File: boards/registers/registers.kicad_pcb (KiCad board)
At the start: 2 copper layers, 100 x 100 mm, 192 parts, among them J1 SSW-120-02-G-D-RA, J2 SSW-120-02-G-D-RA, J4 5V, J5 SSW-120-02-G-D-RA, SW1 RESET, SW2 STEP, SW3 OS102011MS2QN1, U1 SN74ACT08PW, U10 MC74ACT161DG, U11 SN74ACT244PW, U12 SN74ACT244PW, U13 MC74ACT161DG, U14 MC74ACT161DG, U15 SN74ACT244PW, U16 SN74ACT244PW, U17 MC74ACT161DG, U18 MC74ACT161DG, U19 SN74ACT244PW, U2 SN74ACT244PW, U20 SN74ACT244PW, U21 MC74ACT161DG, U22 MC74ACT161DG, U23 SN74ACT244PW, U24 SN74ACT244PW, U25 MC74AC273DTR2G, U26 SN74ACT244PW, U27 SN74ACT244PW, U28 MC74AC273DTR2G, U29 SN74ACT244PW, U3 MC74AC273DTR2G, U34 74ACT14MTCX, U4 MC74ACT161DG, U5 MC74ACT86DG, U6 SN74ACT08PW, U7 SN74ACT32PWR, U8 SN74ACT32PWR, U9 MC74ACT161DG

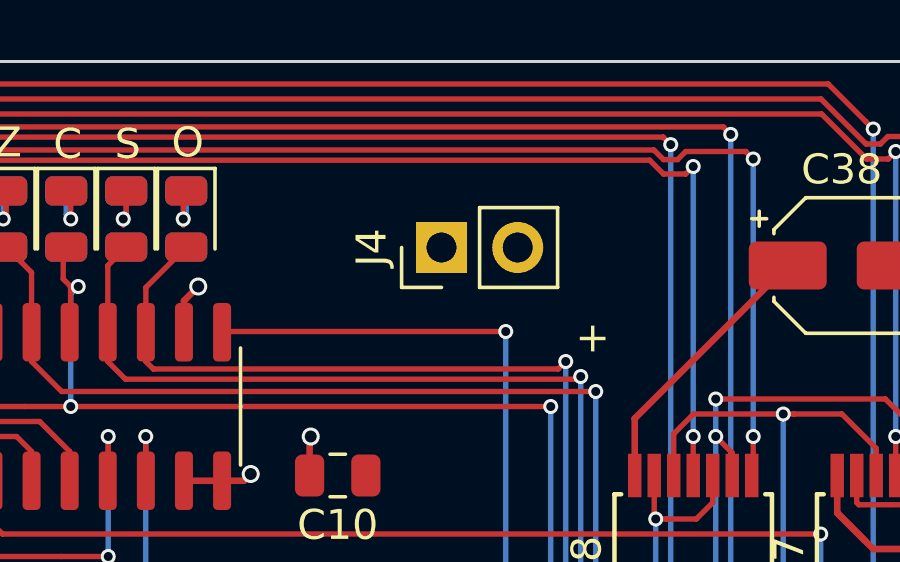
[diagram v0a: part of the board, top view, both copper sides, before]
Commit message: Power connector on the IO board
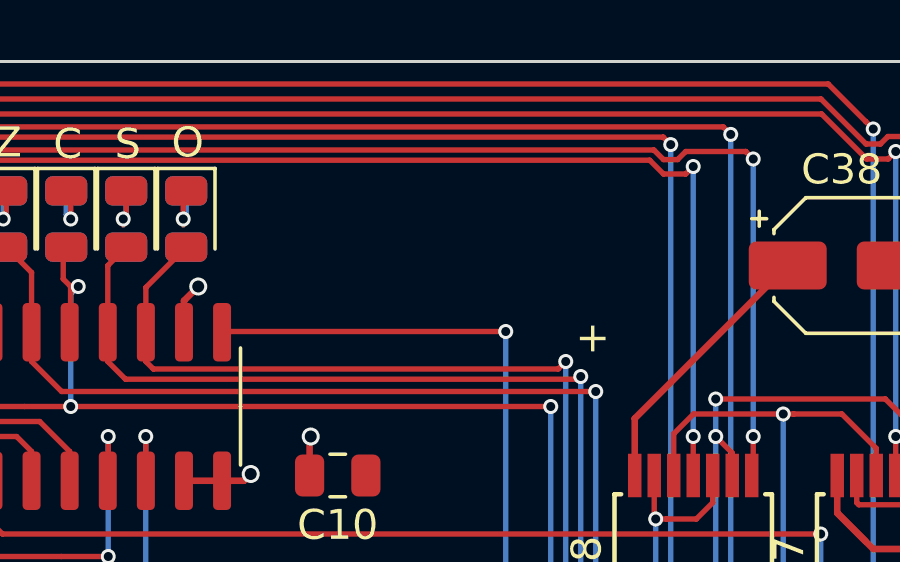
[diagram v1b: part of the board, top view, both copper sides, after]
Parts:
- removed J4: 5V, Connector_PinHeader_2.54mm:PinHeader_1x02_P2.54mm_Vertical
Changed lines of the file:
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@@
     (tracks 5700)
     (zones 0)
-    (modules 192)
+    (modules 191)
     (nets 240)
   )
@@
       (at (xyz 0 0 0))
       (scale (xyz 1 1 1))
-      (rotate (xyz 0 0 0))
-    )
-  )
-  (module Connector_PinHeader_2.54mm:PinHeader_1x02_P2.54mm_Vertical (layer F.Cu)
-    (at 173.86 56.2 90)
-    (descr "Through hole straight pin header, 1x02, 2.54mm pitch, single row")
-    (tags "Through hole pin header THT 1x02 2.54mm single row")
-    (fp_text reference J4 (at 0 -2.33 90) (layer F.SilkS)
-      (effects (font (size 1 1) (thickness 0.15)))
-    )
-    (fp_text value 5V (at 0 4.87 90) (layer F.Fab)
-      (effects (font (size 1 1) (thickness 0.15)))
-    )
-    (fp_line (start -0.635 -1.27) (end 1.27 -1.27) (layer F.Fab) (width 0.1))
-    (fp_line (start 1.27 -1.27) (end 1.27 3.81) (layer F.Fab) (width 0.1))
-    (fp_line (start 1.27 3.81) (end -1.27 3.81) (layer F.Fab) (width 0.1))
-    (fp_line (start -1.27 3.81) (end -1.27 -0.635) (layer F.Fab) (width 0.1))
-    (fp_line (start -1.27 -0.635) (end -0.635 -1.27) (layer F.Fab) (width 0.1))
-    (fp_line (start -1.33 3.87) (end 1.33 3.87) (layer F.SilkS) (width 0.12))
-    (fp_line (start -1.33 1.27) (end -1.33 3.87) (layer F.SilkS) (width 0.12))
-    (fp_line (start 1.33 1.27) (end 1.33 3.87) (layer F.SilkS) (width 0.12))
-    (fp_line (start -1.33 1.27) (end 1.33 1.27) (layer F.SilkS) (width 0.12))
-    (fp_line (start -1.33 0) (end -1.33 -1.33) (layer F.SilkS) (width 0.12))
-    (fp_line (start -1.33 -1.33) (end 0 -1.33) (layer F.SilkS) (width 0.12))
-    (fp_line (start -1.8 -1.8) (end -1.8 4.35) (layer F.CrtYd) (width 0.05))
-    (fp_line (start -1.8 4.35) (end 1.8 4.35) (layer F.CrtYd) (width 0.05))
-    (fp_line (start 1.8 4.35) (end 1.8 -1.8) (layer F.CrtYd) (width 0.05))
-    (fp_line (start 1.8 -1.8) (end -1.8 -1.8) (layer F.CrtYd) (width 0.05))
-    (fp_text user %R (at 0 1.27) (layer F.Fab)
-      (effects (font (size 1 1) (thickness 0.15)))
-    )
-    (pad 1 thru_hole rect (at 0 0 90) (size 1.7 1.7) (drill 1) (layers *.Cu *.Mask)
-      (net 2 GND))
-    (pad 2 thru_hole oval (at 0 2.54 90) (size 1.7 1.7) (drill 1) (layers *.Cu *.Mask)
-      (net 1 VCC))
-    (model ${KISYS3DMOD}/Connector_PinHeader_2.54mm.3dshapes/PinHeader_1x02_P2.54mm_Vertical.wrl
-      (at (xyz 0 0 0))
-      (scale (xyz 1 1 1))

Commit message: Minor update of the registers board
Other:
- board text removed: "+"
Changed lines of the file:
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@@
   (general
     (thickness 1.6)
-    (drawings 29)
+    (drawings 28)
     (tracks 5700)
     (zones 0)
@@
     )
   )
-  (gr_text + (at 178.9 59.2) (layer F.SilkS)
-    (effects (font (size 1 1) (thickness 0.15)))
-  )
   (gr_text "P sel" (at 178.5 105) (layer F.SilkS)
     (effects (font (size 1 1) (thickness 0.15)))
@@
     (effects (font (size 2 2) (thickness 0.3)))
   )
-  (gr_text A (at 161.5 74.5) (layer F.SilkS)
+  (gr_text A (at 162.3 73.9) (layer F.SilkS)
     (effects (font (size 2 2) (thickness 0.3)))
   )
@@
   (segment (start 183.7 105.25) (end 183.7 110.85) (width 0.22) (layer B.Cu) (net 1))
   (segment (start 183.55 111) (end 182.25 111) (width 0.22) (layer F.Cu) (net 1))
-  (segment (start 180.3 61.9) (end 185.4 56.8) (width 0.22) (layer F.Cu) (net 1))
-  (segment (start 180.3 63.8) (end 180.3 61.9) (width 0.22) (layer F.Cu) (net 1))
   (segment (start 190.568 66.25) (end 194.818 62) (width 0.22) (layer F.Cu) (net 1))
   (segment (start 188.25 66.25) (end 190.568 66.25) (width 0.22) (layer F.Cu) (net 1))
   (segment (start 187.05 65.05) (end 188.25 66.25) (width 0.22) (layer F.Cu) (net 1))
+  (segment (start 180.3 63.8) (end 180.3 61.9) (width 0.22) (layer F.Cu) (net 1) (status 1000000))
+  (segment (start 180.3 61.9) (end 185.4 56.8) (width 0.22) (layer F.Cu) (net 1) (status 1000000))
   (via (at 110.25 126.25) (size 0.6) (drill 0.4) (layers F.Cu B.Cu) (net 2))
   (segment (start 110.45 126.05) (end 110.25 126.25) (width 0.22) (layer F.Cu) (net 2))

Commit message: Production files
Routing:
- net GND: track 326.6 -> 348.1 mm
- net VCC: track 439.8 -> 455.3 mm, vias 35 -> 36
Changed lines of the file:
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@@
     (thickness 1.6)
     (drawings 28)
-    (tracks 5700)
+    (tracks 5718)
     (zones 0)
     (modules 191)
@@
       (psa4output false)
       (plotreference true)
-      (plotvalue true)
+      (plotvalue false)
       (plotinvisibletext false)
       (padsonsilk false)
@@
       (outputformat 1)
       (mirror false)
-      (drillshape 1)
+      (drillshape 0)
       (scaleselection 1)
-      (outputdirectory ""))
+      (outputdirectory "production/"))
   )
   (net 0 "")
@@
   (segment (start 188.25 66.25) (end 190.568 66.25) (width 0.22) (layer F.Cu) (net 1))
   (segment (start 187.05 65.05) (end 188.25 66.25) (width 0.22) (layer F.Cu) (net 1))
-  (segment (start 180.3 63.8) (end 180.3 61.9) (width 0.22) (layer F.Cu) (net 1) (status 1000000))
-  (segment (start 180.3 61.9) (end 185.4 56.8) (width 0.22) (layer F.Cu) (net 1) (status 1000000))
+  (segment (start 180.3 63.8) (end 180.3 61.9) (width 0.22) (layer F.Cu) (net 1))
+  (segment (start 180.3 61.9) (end 185.4 56.8) (width 0.22) (layer F.Cu) (net 1))
+  (via (at 172.4 63.8) (size 0.6) (drill 0.4) (layers F.Cu B.Cu) (net 1))
+  (segment (start 172.45 63.85) (end 172.4 63.8) (width 0.22) (layer B.Cu) (net 1))
+  (segment (start 172.45 79.25) (end 172.45 63.85) (width 0.22) (layer B.Cu) (net 1))
   (via (at 110.25 126.25) (size 0.6) (drill 0.4) (layers F.Cu B.Cu) (net 2))
   (segment (start 110.45 126.05) (end 110.25 126.25) (width 0.22) (layer F.Cu) (net 2))
@@
   (segment (start 182.625 117.5) (end 184.875 115.25) (width 0.22) (layer F.Cu) (net 2))
   (segment (start 184.875 115.25) (end 187.5 115.25) (width 0.22) (layer F.Cu) (net 2))
+  (segment (start 156.2125 70.6875) (end 156.2125 73.7125) (width 0.22) (layer B.Cu) (net 2))
+  (segment (start 155.25 70.6875) (end 156.2125 70.6875) (width 0.22) (layer B.Cu) (net 2))
+  (segment (start 156.2125 70.6875) (end 157.25 70.6875) (width 0.22) (layer B.Cu) (net 2))
+  (segment (start 157.25 70.6875) (end 159.25 70.6875) (width 0.22) (layer B.Cu) (net 2))
+  (segment (start 157.95 70.6875) (end 158.2 70.9375) (width 0.22) (layer B.Cu) (net 2))
+  (segment (start 157.25 70.6875) (end 157.95 70.6875) (width 0.22) (layer B.Cu) (net 2))
+  (segment (start 157.25 70.6875) (end 158.3 71.7375) (width 0.22) (layer B.Cu) (net 2))
+  (segment (start 158.3 71.7375) (end 158.3 73.2) (width 0.22) (layer B.Cu) (net 2))
+  (segment (start 159.25 70.6875) (end 161.25 70.6875) (width 0.22) (layer B.Cu) (net 2))
+  (segment (start 161.25 70.6875) (end 163.25 70.6875) (width 0.22) (layer B.Cu) (net 2))
+  (segment (start 163.25 70.6875) (end 165.25 70.6875) (width 0.22) (layer B.Cu) (net 2))
+  (segment (start 161.25 70.6875) (end 162.3 71.7375) (width 0.22) (layer B.Cu) (net 2))
+  (segment (start 162.3 71.7375) (end 162.3 72.7) (width 0.22) (layer B.Cu) (net 2))
+  (segment (start 159.25 70.6875) (end 160.2 71.6375) (width 0.22) (layer B.Cu) (net 2))
+  (segment (start 160.2 71.6375) (end 160.2 72.3) (width 0.22) (layer B.Cu) (net 2))
   (segment (start 182.9 125.9375) (end 183.6 125.9375) (width 0.18) (layer F.Cu) (net 3))
   (segment (start 182.5575 125.9375) (end 182.9 125.9375) (width 0.18) (layer F.Cu) (net 3))

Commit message: Add license information
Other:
- board text added: "Licensed under the TAPR OHL (www.tapr.org/OHL)"
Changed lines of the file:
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@@
   (general
     (thickness 1.6)
-    (drawings 28)
+    (drawings 29)
     (tracks 5718)
     (zones 0)
@@
     (date 2020-02-02)
     (rev 2)
+    (comment 1 "Licensed under the TAPR Open Hardware License (www.tapr.org/OHL)")
   )
   (layers
@@
     )
   )
+  (gr_text "Licensed under the TAPR OHL\n(www.tapr.org/OHL)" (at 179.8 89.7) (layer B.SilkS)
+    (effects (font (size 1 1) (thickness 0.15)) (justify mirror))
+  )
   (gr_text "P sel" (at 178.5 105) (layer F.SilkS)

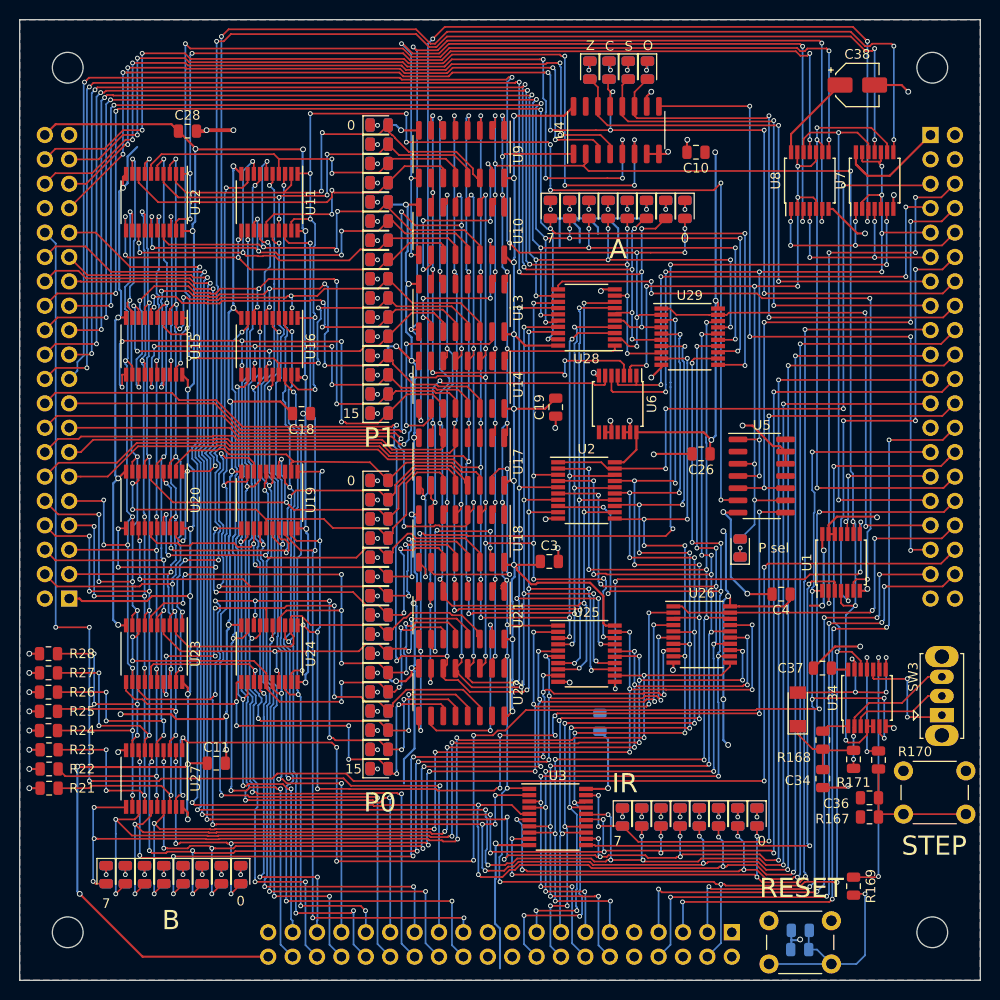
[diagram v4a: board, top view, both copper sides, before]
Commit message: Registers: new board started
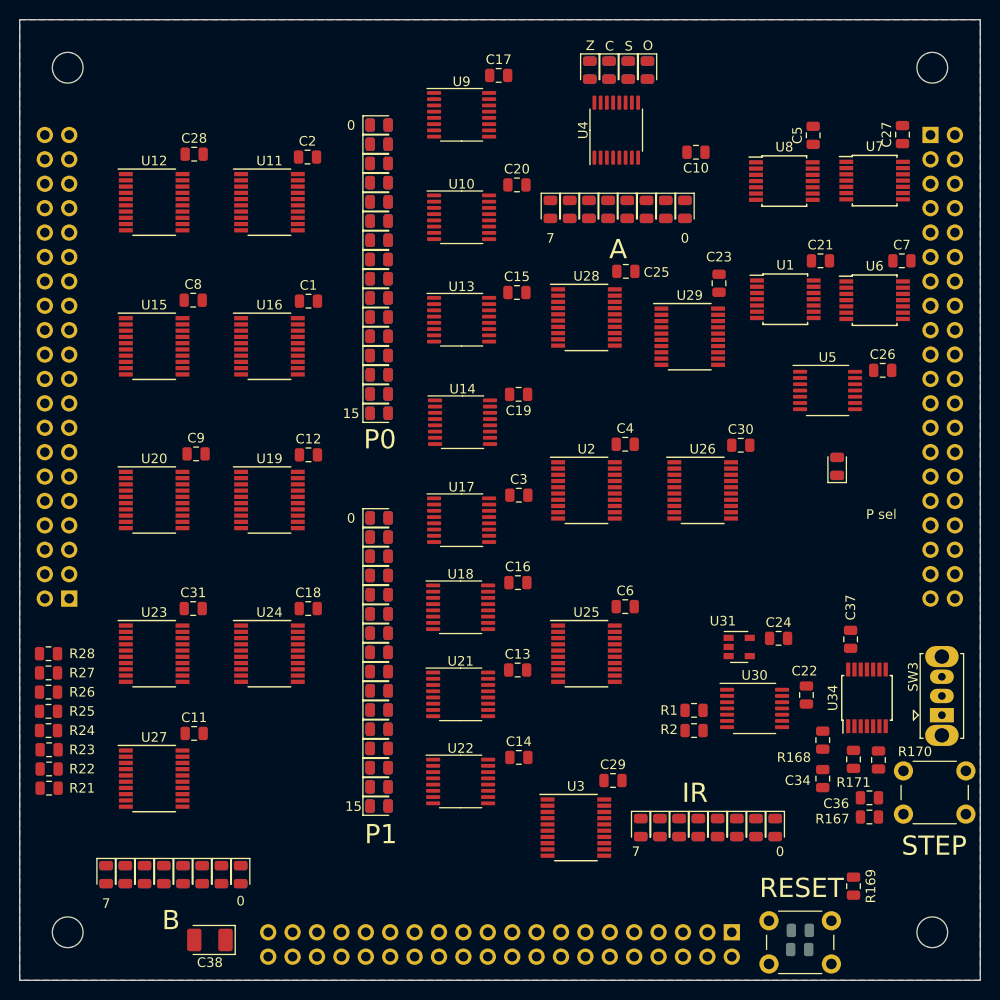
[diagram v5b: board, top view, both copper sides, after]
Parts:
- removed D62: D, Diode_SMD:D_MiniMELF
- added C1: 0.1u, Capacitor_SMD:C_0805_2012Metric, F.Cu at (130.1, 79.3)
- added C12: 0.1u, Capacitor_SMD:C_0805_2012Metric, F.Cu at (130.1, 95.3)
- added C13: 0.1u, Capacitor_SMD:C_0805_2012Metric, F.Cu at (151.8, 117.7)
- added C14: 0.1u, Capacitor_SMD:C_0805_2012Metric, F.Cu at (152.0, 126.8)
- added C15: 0.1u, Capacitor_SMD:C_0805_2012Metric, F.Cu at (151.8, 78.4)
- added C16: 0.1u, Capacitor_SMD:C_0805_2012Metric, F.Cu at (151.9, 108.6)
- added C17: 0.1u, Capacitor_SMD:C_0805_2012Metric, F.Cu at (149.9, 55.8)
- added C2: 0.1u, Capacitor_SMD:C_0805_2012Metric, F.Cu at (130.0, 64.3)
- added C20: 0.1u, Capacitor_SMD:C_0805_2012Metric, F.Cu at (151.8, 67.2)
- added C21: 0.1u, Capacitor_SMD:C_0805_2012Metric, F.Cu at (183.4, 75.1)
- added C22: 0.1u, Capacitor_SMD:C_0805_2012Metric, F.Cu at (181.9, 120.3)
- added C23: 0.1u, Capacitor_SMD:C_0805_2012Metric, F.Cu at (172.8, 77.4)
- added C24: 0.1u, Capacitor_SMD:C_0805_2012Metric, F.Cu at (179.0, 114.4)
- added C25: 0.1u, Capacitor_SMD:C_0805_2012Metric, F.Cu at (163.1, 76.2)
- added C27: 0.1u, Capacitor_SMD:C_0805_2012Metric, F.Cu at (191.9, 62.0)
- added C29: 0.1u, Capacitor_SMD:C_0805_2012Metric, F.Cu at (161.8, 129.2)
- added C30: 0.1u, Capacitor_SMD:C_0805_2012Metric, F.Cu at (175.1, 94.3)
- added C31: 0.1u, Capacitor_SMD:C_0805_2012Metric, F.Cu at (118.1, 111.3)
- added C5: 0.1u, Capacitor_SMD:C_0805_2012Metric, F.Cu at (182.6, 62.0)
- added C7: 0.1u, Capacitor_SMD:C_0805_2012Metric, F.Cu at (191.8, 75.1)
- added C8: 0.1u, Capacitor_SMD:C_0805_2012Metric, F.Cu at (118.1, 79.2)
- added C9: 0.1u, Capacitor_SMD:C_0805_2012Metric, F.Cu at (118.4, 95.2)
- added R1: 22, Resistor_SMD:R_0805_2012Metric, F.Cu at (170.2, 121.9)
- added R2: 22, Resistor_SMD:R_0805_2012Metric, F.Cu at (170.2, 124.0)
- added U30: 74HC74PW, Package_SO:TSSOP-14_4.4x5mm_P0.65mm, F.Cu at (176.5, 121.7)
- added U31: SN74AHC1G86DBVR, Package_TO_SOT_SMD:SOT-23-5, F.Cu at (174.9, 115.3)
- C38: footprint Capacitor_SMD:CP_Elec_4x4.5 -> Capacitor_Tantalum_SMD:CP_EIA-3528-21_Kemet-B_Pad1.50x2.35mm_HandSolder
- C6: moved to F.Cu
- U1, U6: value SN74ACT08PW -> SN74LV08APW
- U10, U13, U14, U17, U18, U21, U22, U4, U9: value MC74ACT161DG -> 74HC161PW; footprint Package_SO:SOIC-16_3.9x9.9mm_P1.27mm -> Package_SO:TSSOP-16_4.4x5mm_P0.65mm
- U11, U12, U15, U16, U19, U2, U20, U23, U24, U26, U27, U29: value SN74ACT244PW -> MC74HC244ADT
- U25, U28, U3: value MC74AC273DTR2G -> MC74HC273ADT
- U34: value 74ACT14MTCX -> SN74LV14APW
- U5: value MC74ACT86DG -> SN74LV86APWR; footprint Package_SO:SOIC-14_3.9x8.7mm_P1.27mm -> Package_SO:TSSOP-14_4.4x5mm_P0.65mm
- U7, U8: value SN74ACT32PWR -> SN74LV32APWR
- moved C38 111.6 mm to (119.8, 145.8), turned to 180 degrees
- moved U6 28.8 mm to (189.0, 79.2), turned to 0 degrees
- moved U1 28.0 mm to (179.7, 79.1), turned to 0 degrees
- moved C4 22.5 mm to (163.0, 94.2), turned to 0 degrees
- moved C26 20.8 mm to (189.8, 86.5), turned to 0 degrees
- moved C18 20.3 mm to (130.0, 111.3), turned to 0 degrees
- moved U26 15.0 mm to (171.1, 99.0)
- moved D13 13.2 mm to (185.1, 96.5)
- moved R29 13.2 mm to (185.1, 96.5)
- moved C6 12.3 mm to (163.0, 111.1), turned to 0 degrees
- moved U5 11.2 mm to (184.1, 88.6)
- moved U22 9.30 mm to (145.9, 129.3), turned to 0 degrees
- moved U21 8.23 mm to (145.9, 120.2), turned to 0 degrees
- moved C3 7.60 mm to (152.0, 99.5)
- moved U18 7.17 mm to (145.9, 111.2), turned to 0 degrees
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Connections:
- J1 pad 34: Net-(J1-Pad34) -> (no net)
- J2 pad 25: Net-(J2-Pad25) -> (no net)
- J2 pad 26: /~mem_rdy -> (no net)
- J2 pad 3: Net-(J2-Pad3) -> (no net)
- J2 pad 4: Net-(J2-Pad4) -> (no net)
- J5 pad 10: Net-(J5-Pad10) -> (no net)
- J5 pad 19: Net-(J5-Pad19) -> (no net)
- J5 pad 20: Net-(J5-Pad20) -> (no net)
- J5 pad 21: Net-(J5-Pad21) -> (no net)
- J5 pad 22: Net-(J5-Pad22) -> (no net)
- J5 pad 4: /~rst -> /~ext_rst
- J5 pad 5: /~mem_rdy -> /mem_rdy
- J5 pad 6: Net-(J5-Pad6) -> (no net)
- J5 pad 9: Net-(J5-Pad9) -> (no net)
- SW3 pad 2: Net-(SW3-Pad2) -> /pwr_and_clk/src_clk
- U1 pad 1: /clk -> /~clk
- U1 pad 11: Net-(U1-Pad11) -> (no net)
- U1 pad 12: GND -> VCC
- U1 pad 13: GND -> VCC
- U14 pad 15: Net-(U14-Pad15) -> (no net)
- U22 pad 15: Net-(U22-Pad15) -> (no net)
- U34 pad 10: Net-(SW3-Pad1) -> /~ext_rst
- U34 pad 11: Net-(R170-Pad1) -> Net-(U34-Pad11)
- U34 pad 12: /~rst -> (no net)
- U34 pad 13: Net-(D62-Pad2) -> VCC
- U34 pad 3: Net-(SW3-Pad2) -> Net-(R169-Pad1)
- U34 pad 4: /~clk -> Net-(U34-Pad11)
- U34 pad 5: /~clk -> Net-(U34-Pad11)
- U34 pad 6: /clk -> /~rst
- U34 pad 8: Net-(D62-Pad2) -> Net-(SW3-Pad1)
- U34 pad 9: Net-(R169-Pad1) -> Net-(R170-Pad1)
- U4 pad 15: Net-(U4-Pad15) -> (no net)
- U5 pad 11: Net-(U5-Pad11) -> (no net)
- U5 pad 12: GND -> VCC
- U5 pad 13: GND -> VCC
- U6 pad 10: GND -> Net-(U6-Pad10)
- U6 pad 11: Net-(U6-Pad11) -> Net-(U6-Pad10)
- U6 pad 12: GND -> VCC
- U6 pad 13: GND -> VCC
- U6 pad 8: Net-(U6-Pad8) -> (no net)
- U6 pad 9: GND -> Net-(U6-Pad10)
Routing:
- net VCC: track 455.3 -> 0.00 mm, vias 36 -> 0
- net GND: track 348.1 -> 0.00 mm, vias 59 -> 0
- net /~rst: track 223.6 -> 0.00 mm, vias 16 -> 0
- net /alu_invert: track 221.2 -> 0.00 mm, vias 8 -> 0
- net /alu_op0: track 219.6 -> 0.00 mm, vias 10 -> 0
- net /alu_op3: track 216.8 -> 0.00 mm, vias 10 -> 0
- net /alu_op1: track 212.2 -> 0.00 mm, vias 10 -> 0
- net /alu_op2: track 211.2 -> 0.00 mm, vias 10 -> 0
- net /di7: track 194.4 -> 0.00 mm, vias 12 -> 0
- net /di6: track 189.0 -> 0.00 mm, vias 13 -> 0
- net /di5: track 178.5 -> 0.00 mm, vias 12 -> 0
- net /~clk: track 174.9 -> 0.00 mm, vias 13 -> 0
- net /~oe_alu: track 174.8 -> 0.00 mm, vias 5 -> 0
- net /di3: track 161.7 -> 0.00 mm, vias 8 -> 0
- net /di2: track 159.8 -> 0.00 mm, vias 9 -> 0
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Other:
- net class Clock added: clearance 0.5, trace_width 0.16, via_dia 0.5, via_drill 0.3
- net class Default: trace_width 0.18 -> 0.16

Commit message: Registers: power tracks
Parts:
- moved C10 13.9 mm to (157.4, 59.0)
- moved C4 1.80 mm to (163.0, 92.4)
- moved U2 1.80 mm to (159.0, 97.2)
- moved D13 1.25 mm to (184.0, 95.9)
- moved R29 1.25 mm to (184.0, 95.9)
- moved C36 1.20 mm to (187.3, 131.0)
- moved R167 1.20 mm to (187.3, 133.0)
- moved R170 1.20 mm to (188.2, 127.1)
- moved R171 1.20 mm to (185.6, 127.0)
- moved C34 1.20 mm to (182.4, 129.0)
- moved R168 1.20 mm to (182.4, 125.0)
- moved SW2 1.20 mm to (190.8, 128.2)
- moved C37 1.10 mm to (185.4, 114.6)
- moved C7 1.04 mm to (190.8, 75.2), turned to 180 degrees
- moved U34 1.00 mm to (187.2, 120.7)
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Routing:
- net GND: track 0.00 -> 1389.6 mm, vias 0 -> 68
- net VCC: track 0.00 -> 954.3 mm, vias 0 -> 40
